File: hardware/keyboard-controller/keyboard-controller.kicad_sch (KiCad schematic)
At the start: 19 parts, among them J1 Keybed_Connector, U1 Pico, U2 MCP4921, U3 TL431LP, U4 74HC164, U5 74HC164, U6 LM358

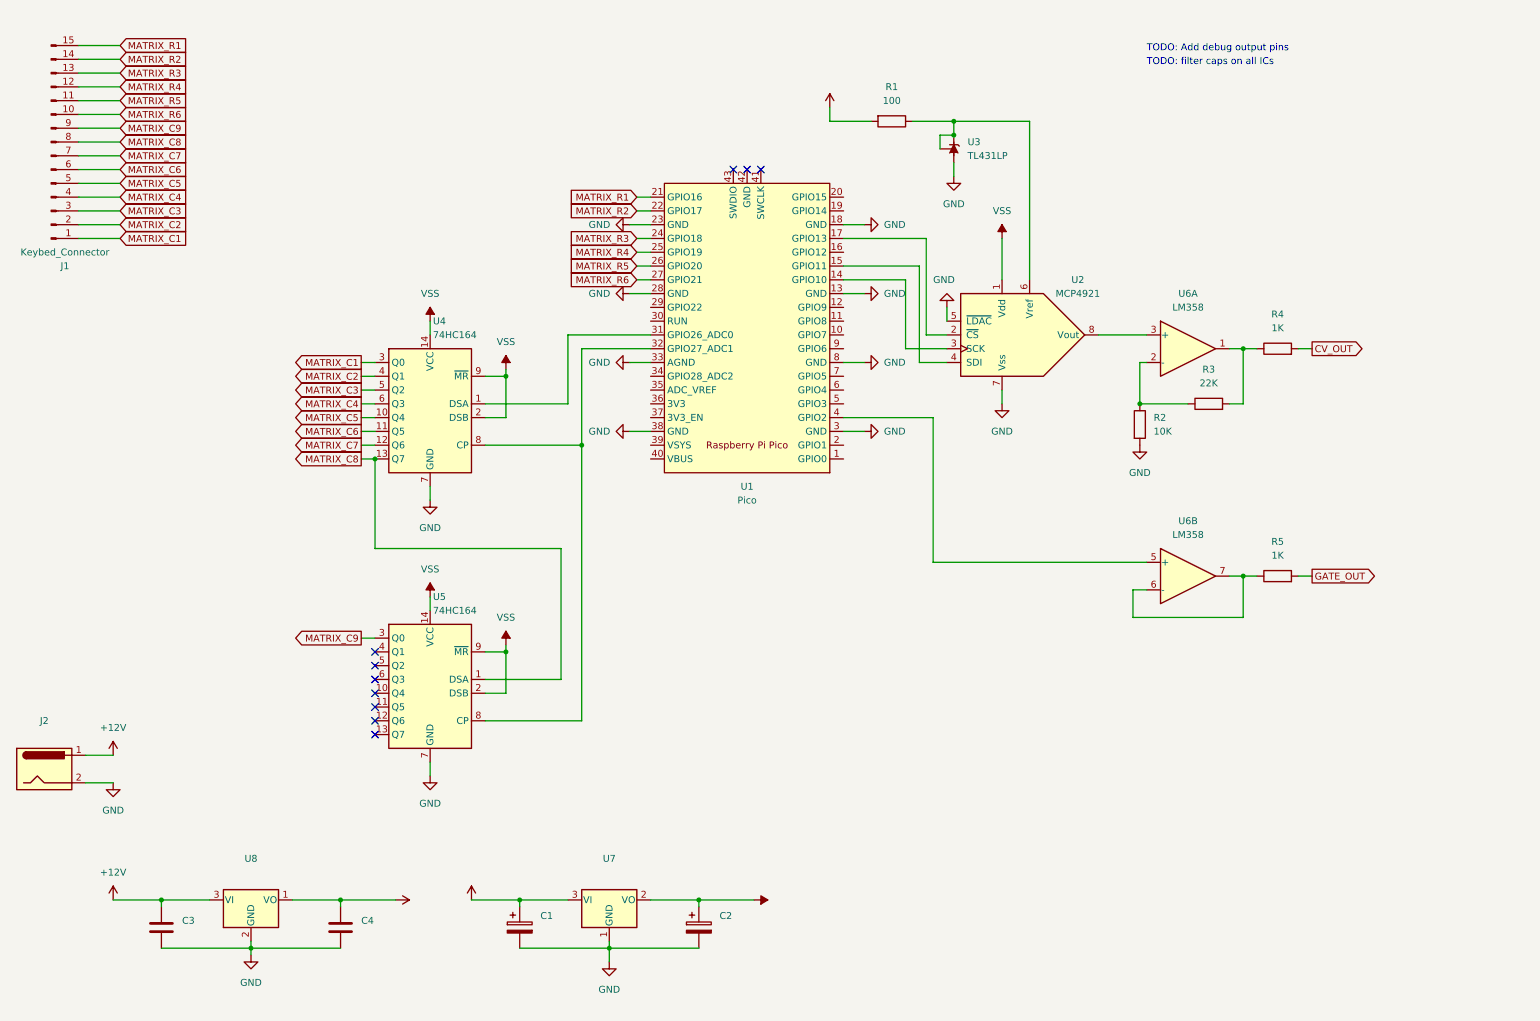
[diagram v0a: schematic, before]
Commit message: Reorganized hardware folder to keep libraries locally. Added footprints to most symbols
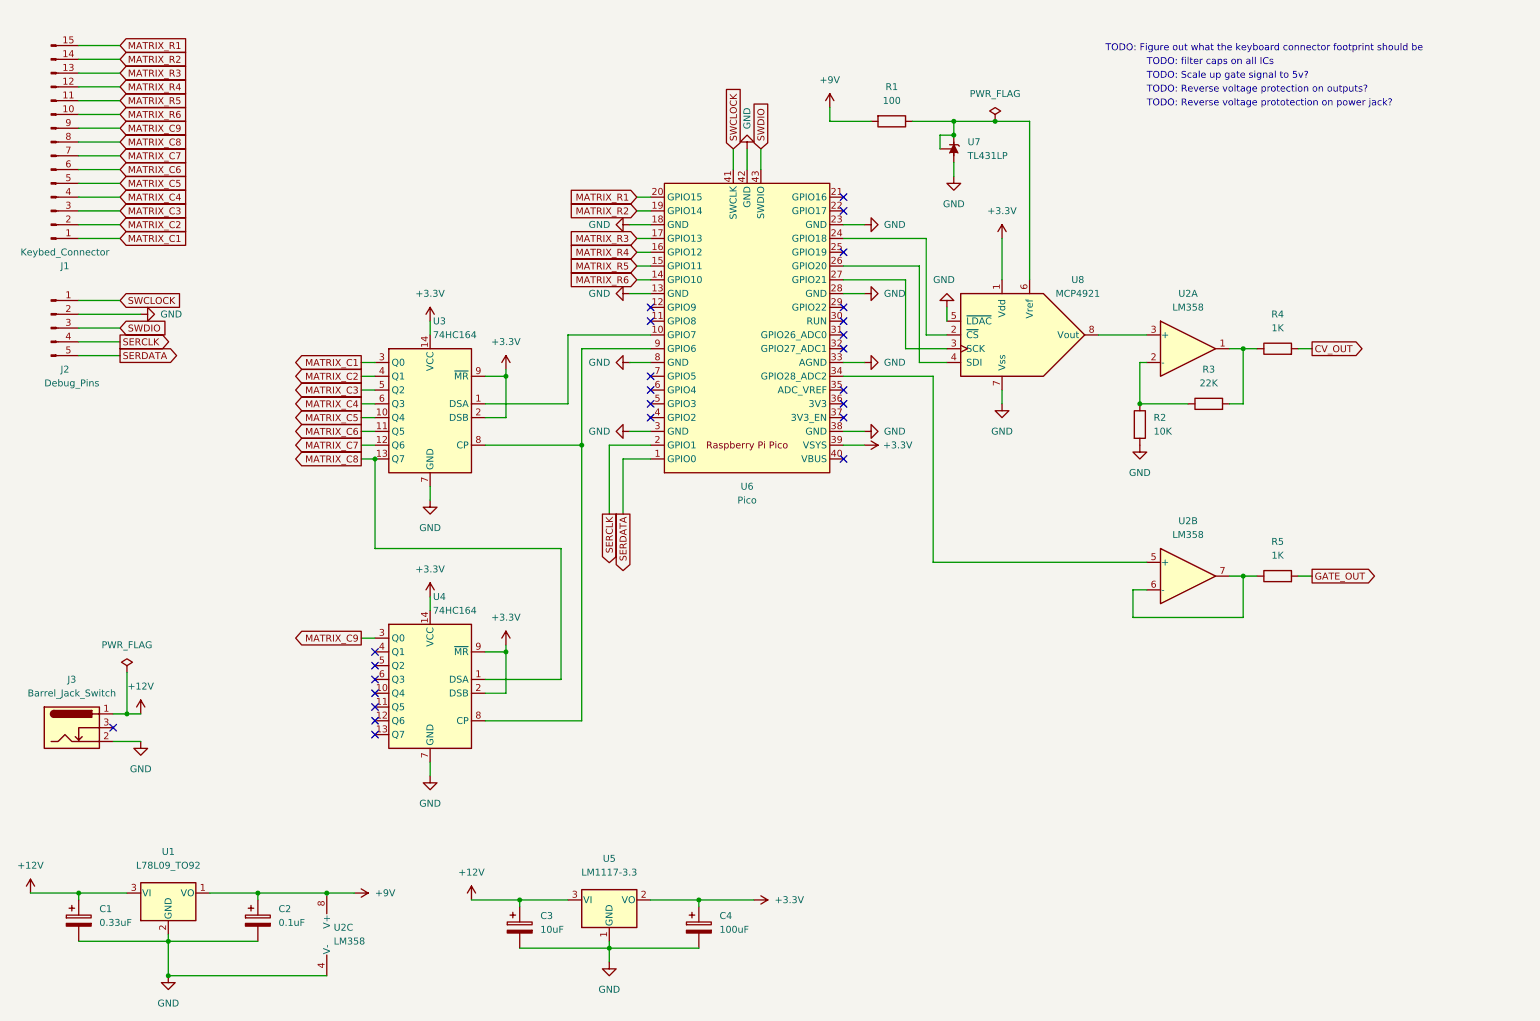
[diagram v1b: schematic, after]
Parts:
- removed J2: (no value), symbol Connector:Barrel_Jack
- added J2: Debug_Pins, Connector_PinHeader_2.54mm:PinHeader_1x05_P2.54mm_Vertical, symbol Connector:Conn_01x05_Male
- added J3: Barrel_Jack_Switch, symbol Connector:Barrel_Jack_Switch
- added unit 3 of U2
- C1: renamed from C3; value (none) -> 0.33uF; footprint (none) -> Capacitor_THT:CP_Radial_Tantal_D4.5mm_P2.50mm; symbol Device:C -> Device:C_Polarized
- C2: renamed from C4; value (none) -> 0.1uF; footprint (none) -> Capacitor_THT:CP_Radial_Tantal_D4.5mm_P2.50mm; symbol Device:C -> Device:C_Polarized
- C3: renamed from C1; value (none) -> 10uF; footprint (none) -> Capacitor_THT:CP_Radial_Tantal_D4.5mm_P2.50mm
- C4: renamed from C2; value (none) -> 100uF; footprint (none) -> Capacitor_THT:CP_Radial_Tantal_D4.5mm_P2.50mm
- J1: footprint (none) -> Connector_PinHeader_2.54mm:PinHeader_1x15_P2.54mm_Vertical
- R1, R2, R3, R4, R5: footprint (none) -> Royal_Ohm_Resistors:R_Axial_DIN0207_L6.8mm_D2.5mm_P10.16mm_Horizontal
- U1: renamed from U8; value (none) -> L78L09_TO92; footprint (none) -> Package_TO_SOT_THT:TO-92_Inline
- U2: renamed from U6; footprint (none) -> Package_DIP:DIP-8_W7.62mm_Socket
- U3: renamed from U4; footprint (none) -> Package_DIP:DIP-14_W7.62mm_Socket
- U4: renamed from U5; footprint (none) -> Package_DIP:DIP-14_W7.62mm_Socket
- U5: renamed from U7; value (none) -> LM1117-3.3; footprint (none) -> Package_TO_SOT_THT:TO-220-3_Horizontal_TabDown
- U6: renamed from U1; footprint RPi_Pico:RPi_Pico_SMD_TH -> (none)
- U8: renamed from U2; footprint (none) -> Package_DIP:DIP-8_W7.62mm_Socket
- renumbered U3 to U7
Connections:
- net VSS is gone; now on net +3V3: C4.1, U3.14 (VCC), U3.2 (DSB), U3.9 (~{MR}), U4.14 (VCC), U4.2 (DSB), U4.9 (~{MR}), U5.2 (VO), U8.1 (Vdd)
- net +12V: now also J3.1
- net +9V: now also U2.8 (V+)
- net GND: now also U6.42 (GND), J2.2 (Pin_2), J3.2, U2.4 (V-)
- net MATRIX_R1: now also U6.20 (GPIO15); no longer U6.21 (GPIO16)
- net MATRIX_R2: now also U6.19 (GPIO14); no longer U6.22 (GPIO17)
- net MATRIX_R3: now also U6.17 (GPIO13); no longer U6.24 (GPIO18)
- net MATRIX_R4: now also U6.16 (GPIO12); no longer U6.25 (GPIO19)
- net MATRIX_R5: now also U6.15 (GPIO11); no longer U6.26 (GPIO20)
- net MATRIX_R6: now also U6.14 (GPIO10); no longer U6.27 (GPIO21)
- net at U2.5 (+): now also U6.34 (GPIO28_ADC2); no longer U6.4 (GPIO2)
- net SERDATA: now reaches U6.1 (GPIO0)
- net SERDATA: now also J2.5 (Pin_5)
- net at U6.10 (GPIO7): now also U3.1 (DSA)
- net at U8.3 (SCK): now also U6.27 (GPIO21); no longer U6.14 (GPIO10)
- net at U8.4 (SDI): now also U6.26 (GPIO20); no longer U6.15 (GPIO11)
- net at U8.2 (~{CS}): now also U6.24 (GPIO18); no longer U6.17 (GPIO13)
- net SERCLK: now reaches U6.2 (GPIO1)
- net SERCLK: now also J2.4 (Pin_4)
- net at U6.31 (GPIO26_ADC0): no longer U3.1 (DSA)
- net at U3.8 (CP), U4.8 (CP): now also U6.9 (GPIO6); no longer U6.32 (GPIO27_ADC1)
- net +3V3: now reaches U6.39 (VSYS)
- net SWCLOCK: now reaches U6.41 (SWCLK)
- net SWCLOCK: now also J2.1 (Pin_1)
- net SWDIO: now reaches U6.43 (SWDIO)
- net SWDIO: now also J2.3 (Pin_3)
- no-connect marks 10 -> 25
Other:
- note added: "TODO: Figure out what the keyboard connector footprint should be"
- note added: "TODO: Reverse voltage protection on outputs?"
- note added: "TODO: Reverse voltage prototection on power jack?"
- note added: "TODO: Scale up gate signal to 5v?"
- note removed: "TODO: Add debug output pins"
- moved on the sheet: U1, U6

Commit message: Added cv/gate output jacks
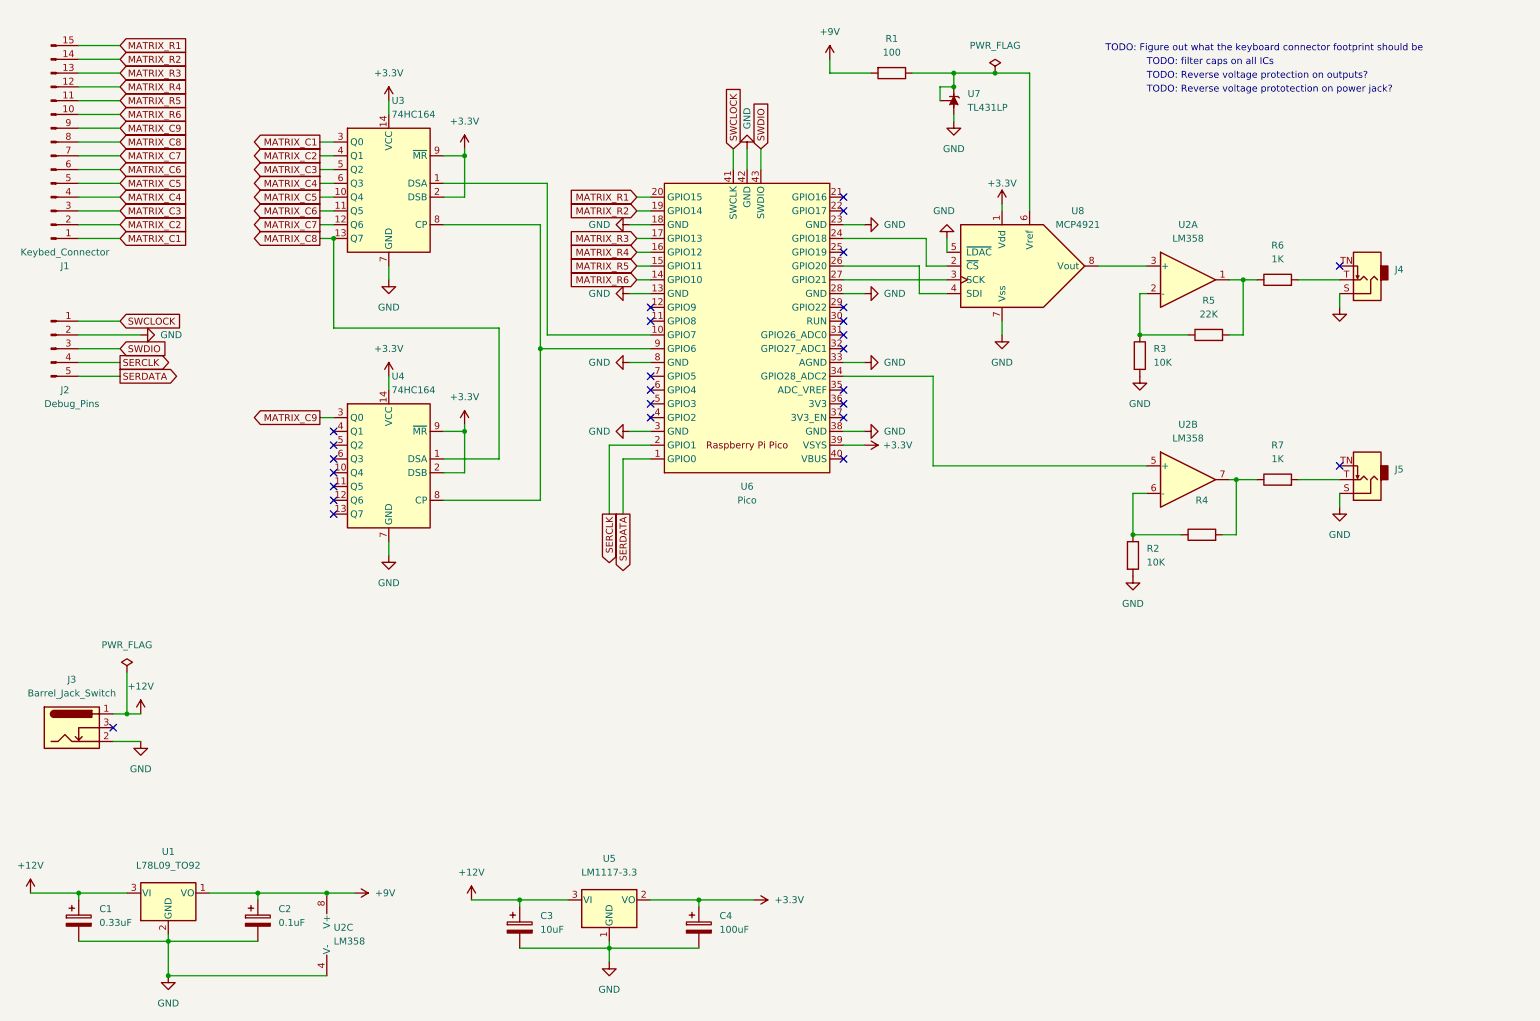
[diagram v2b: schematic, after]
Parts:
- added J4, J5: (no value), symbol Connector:AudioJack2_SwitchT
- added R2: 10K, Royal_Ohm_Resistors:R_Axial_DIN0207_L6.8mm_D2.5mm_P10.16mm_Horizontal, symbol Device:R
- added R4: (no value), Royal_Ohm_Resistors:R_Axial_DIN0207_L6.8mm_D2.5mm_P10.16mm_Horizontal, symbol Device:R
- renumbered R2 to R3, R3 to R5, R4 to R6, R5 to R7
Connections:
- net GND: now also J4.S, J5.S, R2.2
- net at R7.1, U2.7: now also R4.2; no longer U2.6 (-)
- net CV_OUT: no longer names the net of R6.2
- net CV_OUT: now also J4.T
- net GATE_OUT: no longer names the net of R7.2
- net GATE_OUT: now also J5.T
- new net: R2.1, R4.1, U2.6 (-)
- no-connect marks 25 -> 27
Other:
- note removed: "TODO: Scale up gate signal to 5v?"
- moved on the sheet: J2, R1, R3, R5, R6, R7, U2A, U2B, U3, U4, U7, U8

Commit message: Schematic updates: Added filter caps on all ICs, resolved some TODOs
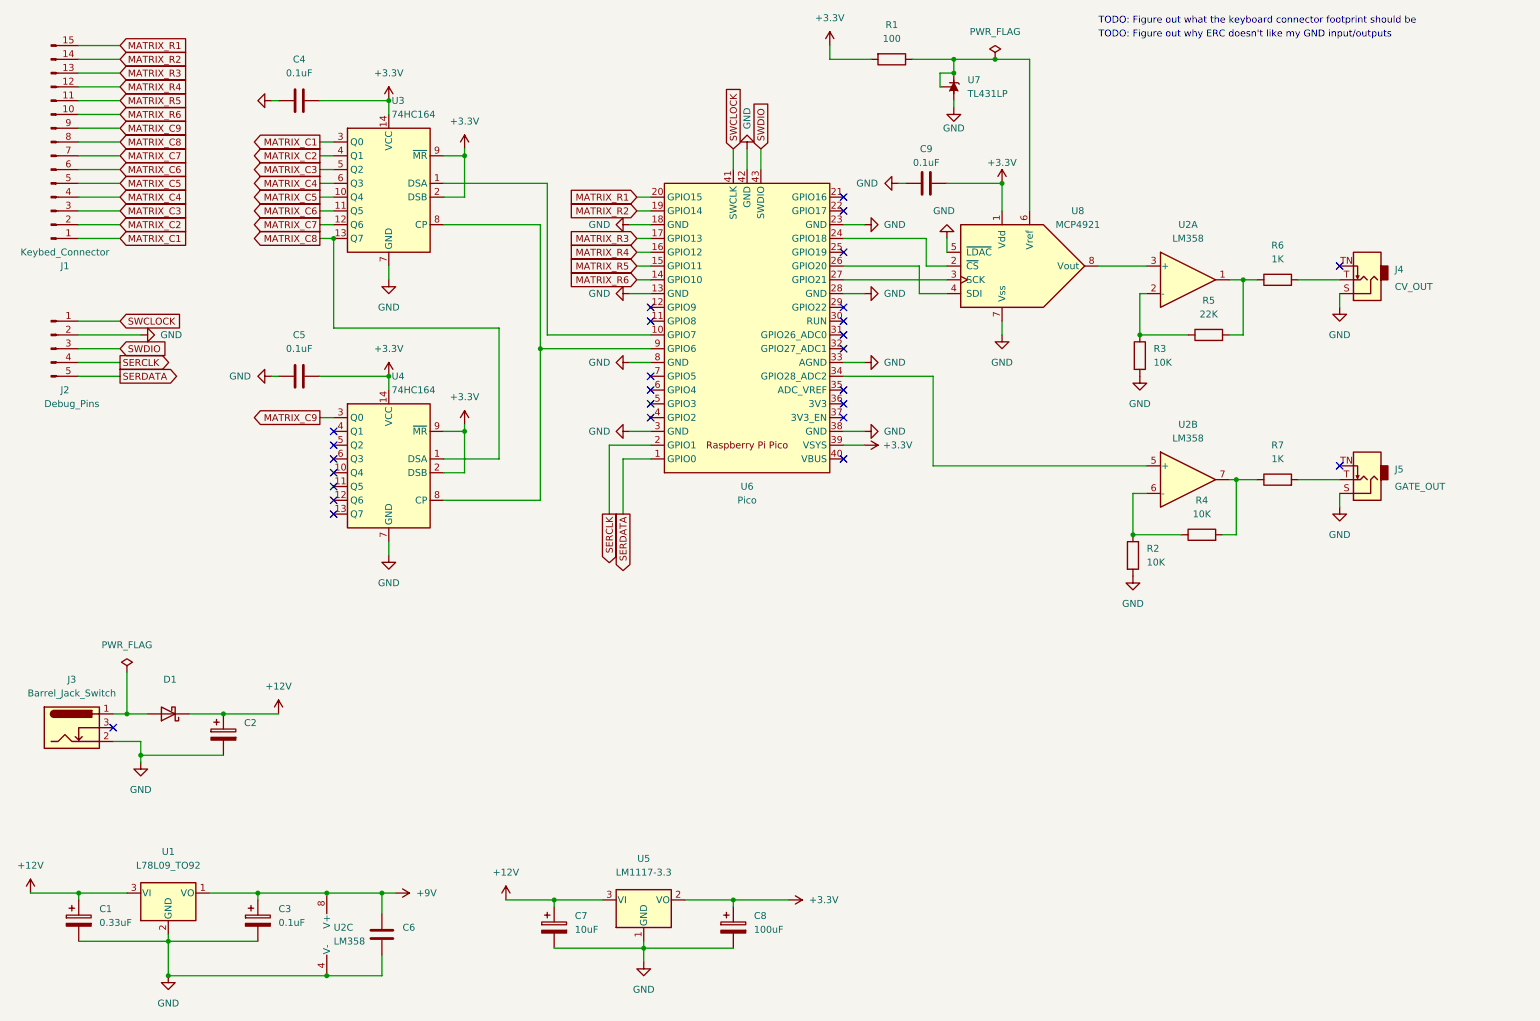
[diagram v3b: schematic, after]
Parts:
- added C2: (no value), symbol Device:C_Polarized
- added C4, C5, C9: 0.1uF, AEC_Capacitors:C_Disc_D5.0mm_W2.5mm_P3.0mm, symbol Device:C
- added C6: (no value), symbol Device:C
- added D1: (no value), symbol Diode:1N5818
- J3: footprint (none) -> WEALTH_METAL_Barrel_Jacks:BarrelJack_Horizontal_2.1mm_WEALTH_METAL
- J4: value (none) -> CV_OUT; footprint (none) -> AudioJacks:Jack_3.5mm_QingPu_WQP-PJ398SM_Vertical
- J5: value (none) -> GATE_OUT; footprint (none) -> AudioJacks:Jack_3.5mm_QingPu_WQP-PJ398SM_Vertical
- R4: value (none) -> 10K
- U6: footprint (none) -> MCU_RaspberryPi_and_Boards:RPi_Pico_SMD_TH
- renumbered C2 to C3, C3 to C7, C4 to C8
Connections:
- net +12V: now also C2.1, D1.1 (K); no longer J3.1
- net +3V3: now also R1.2, C4.2, C5.2, C9.2
- net +9V: now also C6.1; no longer R1.2
- net GND: now also C2.2, C4.1, C5.1, C6.2, C9.1
- new net: D1.2 (A), J3.1
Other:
- note added: "TODO: Figure out why ERC doesn't like my GND input/outputs"
- note removed: "TODO: Reverse voltage protection on outputs?"
- note removed: "TODO: Reverse voltage prototection on power jack?"
- note removed: "TODO: filter caps on all ICs"
- moved on the sheet: C7, C8, R1, U5, U7

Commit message: Fixed shift register <-> pico pins in schematic. Moved shift register clk/data pins
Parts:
- C2: value (none) -> 47uF; footprint (none) -> Capacitor_THT:CP_Radial_D5.0mm_P2.00mm
- C6: value (none) -> 0.1uF; footprint (none) -> AEC_Capacitors:C_Disc_D5.0mm_W2.5mm_P3.0mm
- D1: value (none) -> 1N5818; footprint (none) -> Diode_THT:D_DO-41_SOD81_P10.16mm_Horizontal
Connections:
- net MATRIX_R1: now also U6.21 (GPIO16); no longer U6.20 (GPIO15)
- net MATRIX_R2: now also U6.22 (GPIO17); no longer U6.19 (GPIO14)
- net MATRIX_R3: now also U6.24 (GPIO18); no longer U6.17 (GPIO13)
- net MATRIX_R4: now also U6.25 (GPIO19); no longer U6.16 (GPIO12)
- net MATRIX_R5: now also U6.26 (GPIO20); no longer U6.15 (GPIO11)
- net MATRIX_R6: now also U6.27 (GPIO21); no longer U6.14 (GPIO10)
- net at U2.5 (+): now also U6.7 (GPIO5); no longer U6.34 (GPIO28_ADC2)
- net at U6.10 (GPIO7): no longer U3.1 (DSA)
- net at U8.2 (~{CS}): now also U6.17 (GPIO13); no longer U6.24 (GPIO18)
- net at U8.4 (SDI): now also U6.15 (GPIO11); no longer U6.26 (GPIO20)
- net at U8.3 (SCK): now also U6.14 (GPIO10); no longer U6.27 (GPIO21)
- net at U6.29 (GPIO22): now also U3.1 (DSA)
- net at U6.31 (GPIO26_ADC0): now also U3.8 (CP), U4.8 (CP)
- now unconnected: U6.9 (GPIO6)
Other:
- note added: "TODO: Add octave buttons: https://www.sparkfun.com/products/9190"
- note added: "TODO: Change keyboard connector footprint to 16pin IDC"
- note added: "TODO: The LM1117 Tab is Vout!"
- note removed: "TODO: Figure out what the keyboard connector footprint should be"
- moved on the sheet: U6
